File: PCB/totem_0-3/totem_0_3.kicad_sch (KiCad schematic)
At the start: 88 parts, among them J1 MJ-4PP-9, J2 MJ-4PP-9, U1 xiao-ble, U2 xiao-ble

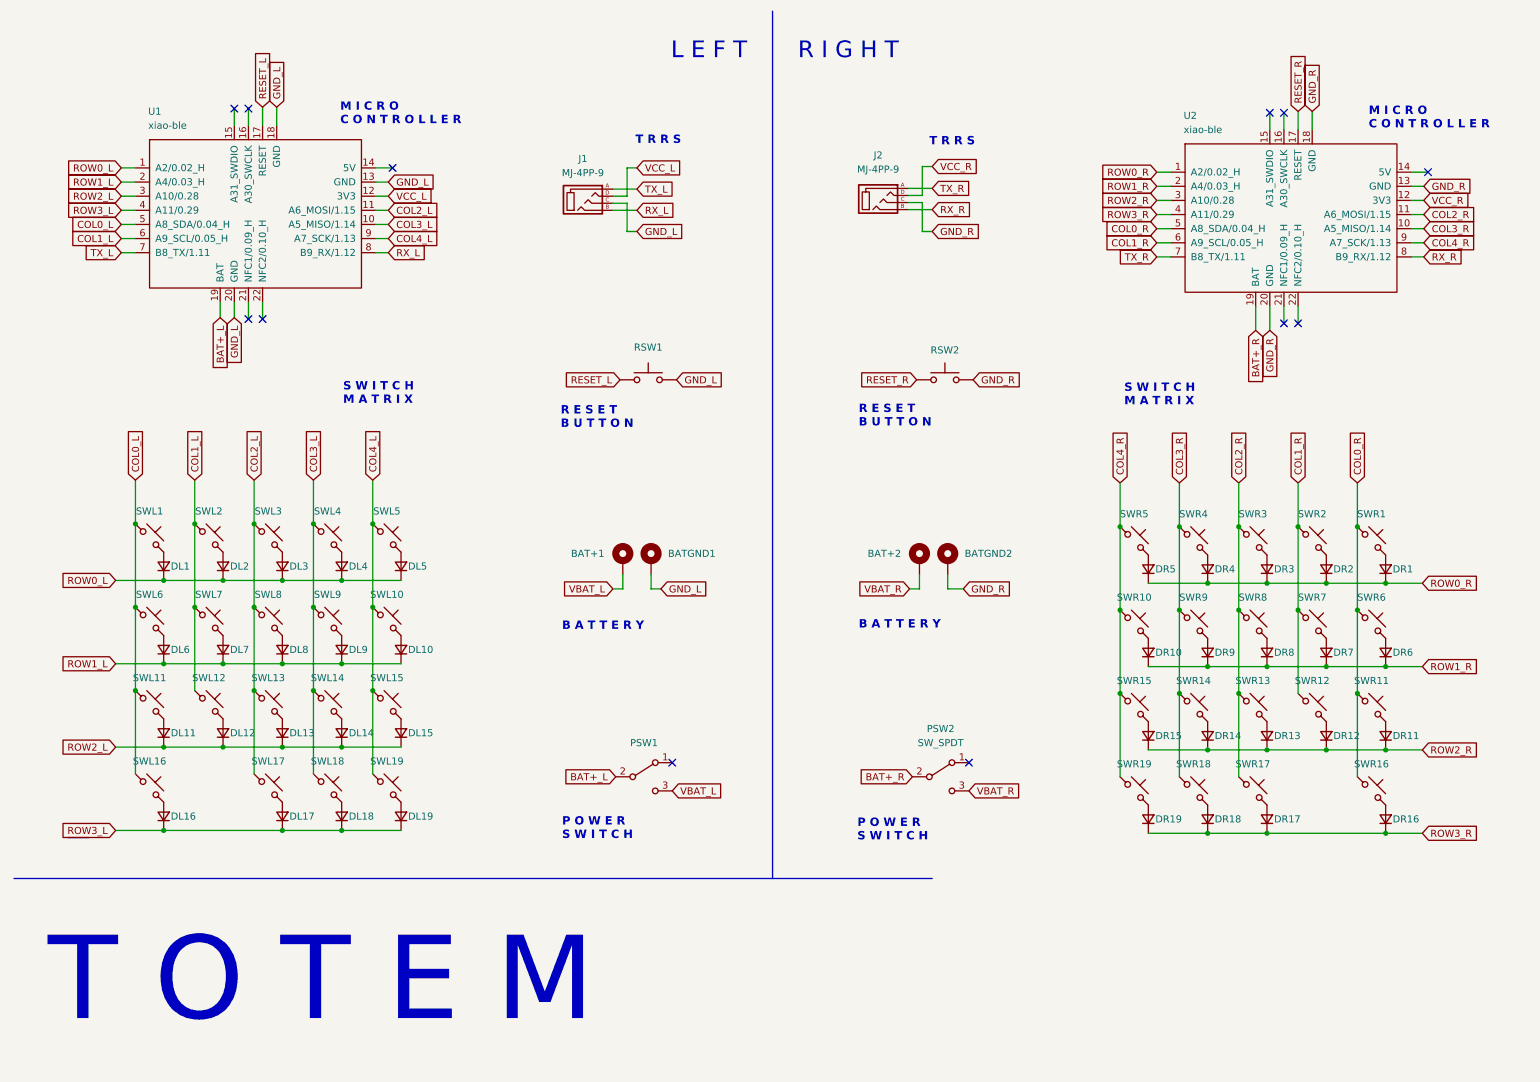
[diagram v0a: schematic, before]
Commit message: Modded for nice-nano
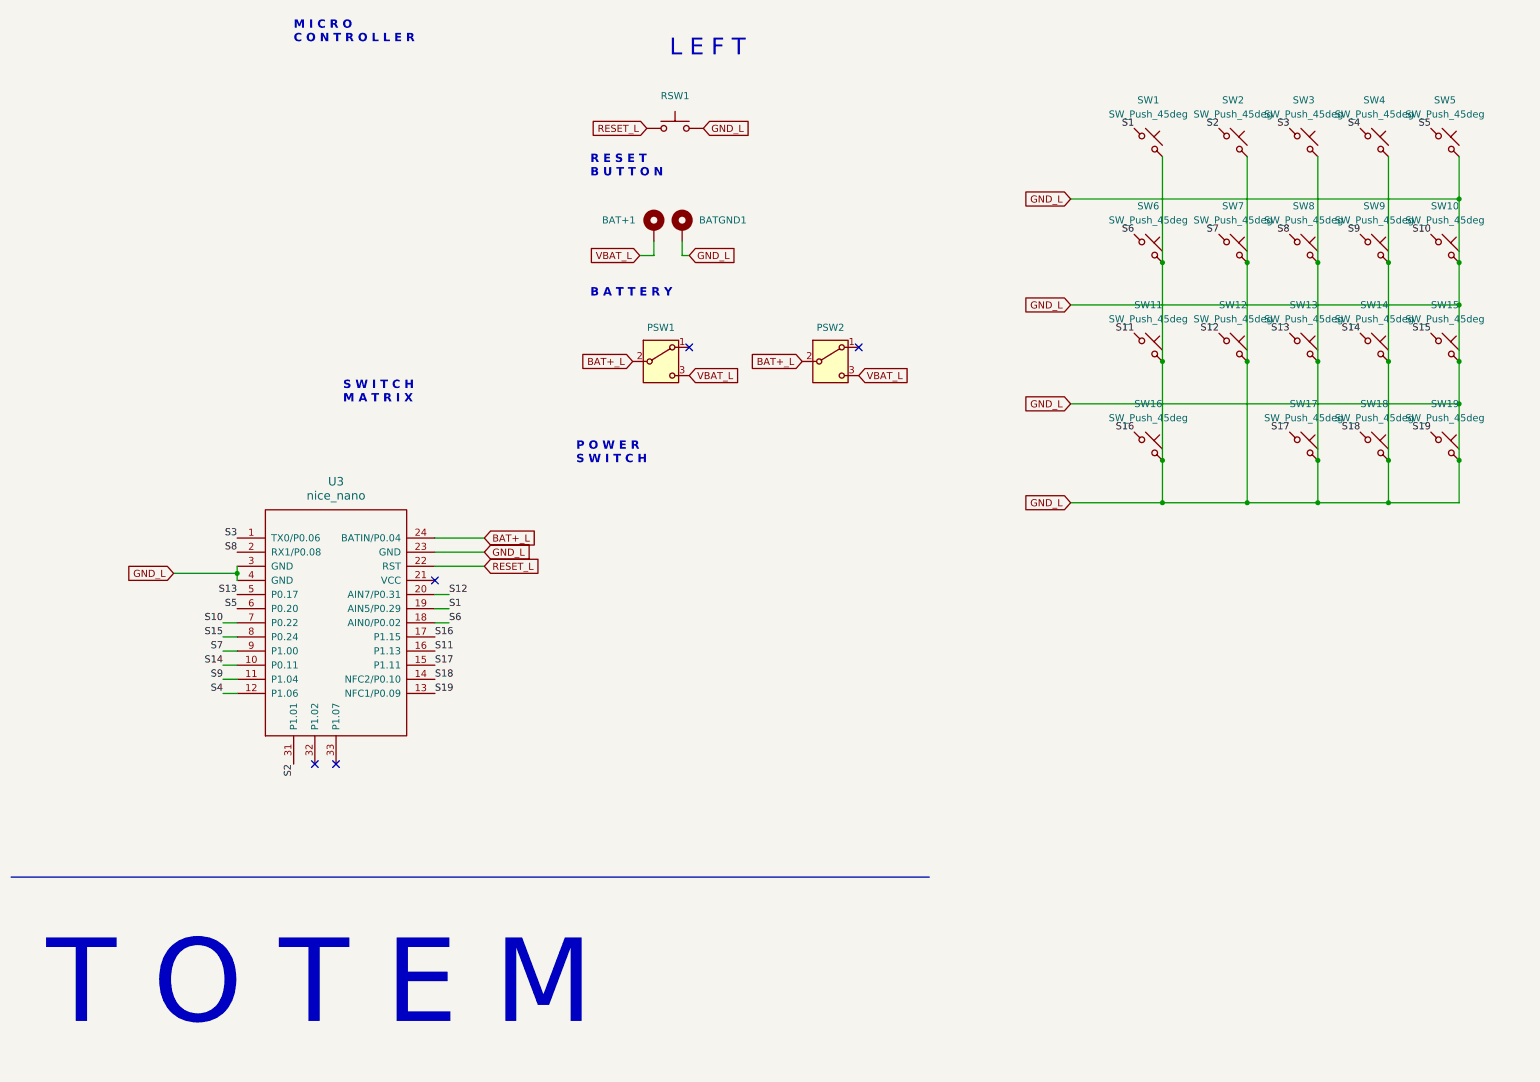
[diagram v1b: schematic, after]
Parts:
- removed BAT+2: +, TOTEMlib:BatteryPad, symbol Mechanical:MountingHole_Pad
- removed BATGND2: -, TOTEMlib:BatteryPad, symbol Mechanical:MountingHole_Pad
- removed DL1, DL10, DL11, DL12, DL13, DL14, DL15, DL16, DL17, DL18, DL19, DL2, DL3, DL4, DL5, DL6, DL7, DL8, DL9, DR1, DR10, DR11, DR12, DR13, DR14, DR15, DR16, DR17, DR18, DR19, DR2, DR3, DR4, DR5, DR6, DR7, DR8, DR9: D_Small, TOTEMlib:Diode_SOD123, symbol Device:D_Small
- removed J1, J2: MJ-4PP-9, TOTEMlib:MJ-4PP-9_1side, symbol kbd:MJ-4PP-9
- removed RSW2: SW_Push, TOTEMlib:SKHLLCA010, symbol Switch:SW_Push
- removed SWL1, SWL10, SWL11, SWL12, SWL13, SWL14, SWL15, SWL16, SWL17, SWL18, SWL19, SWL2, SWL3, SWL4, SWL5, SWL6, SWL7, SWL8, SWL9, SWR1, SWR10, SWR11, SWR12, SWR13, SWR14, SWR15, SWR16, SWR17, SWR18, SWR19, SWR2, SWR3, SWR4, SWR5, SWR6, SWR7, SWR8, SWR9: SW_Push_45deg, TOTEMlib:Kailh_socket_PG1350_optional, symbol Switch:SW_Push_45deg
- removed U1, U2: xiao-ble, TOTEMlib:xiao-ble-smd-cutout, symbol mcu:xiao-ble
- added SW1, SW10, SW11, SW12, SW13, SW14, SW15, SW16, SW17, SW18, SW19, SW2, SW3, SW4, SW5, SW6, SW7, SW8, SW9: SW_Push_45deg, switches:Kailh_socket_PG1350_reversible, symbol Switch:SW_Push_45deg
- added U3: nice_nano, nice-nano:nice_nano, symbol nice-nano:nice_nano
- BAT+1, BATGND1: now left out of the parts list
- RSW1: footprint TOTEMlib:SKHLLCA010 -> kbd:ResetSW
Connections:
- net BAT+_R is gone; now on net BAT+_L: PSW2.2 (B)
- net VBAT_R is gone; now on net VBAT_L: PSW2.3 (C)
- net BAT+_L: now also U3.24 (BATIN/P0.04)
- net GND_L: now also SW1.2, SW10.2, SW11.2, SW12.2, SW13.2, SW14.2, SW15.2, SW16.2, SW17.2, SW18.2, SW19.2, SW2.2, SW3.2, SW4.2, SW5.2, SW6.2, SW7.2, SW8.2, SW9.2, U3.23 (GND), U3.3 (GND), U3.4 (GND)
- net RESET_L: now also U3.22 (RST)
- new net S1: SW1.1, U3.19 (AIN5/P0.29)
- new net S10: SW10.1, U3.7 (P0.22)
- new net S11: SW11.1, U3.16 (P1.13)
- new net S12: SW12.1, U3.20 (AIN7/P0.31)
- new net S13: SW13.1, U3.5 (P0.17)
- new net S14: SW14.1, U3.10 (P0.11)
- new net S15: SW15.1, U3.8 (P0.24)
- new net S16: SW16.1, U3.17 (P1.15)
- new net S17: SW17.1, U3.15 (P1.11)
- new net S18: SW18.1, U3.14 (NFC2/P0.10)
- new net S19: SW19.1, U3.13 (NFC1/P0.09)
- new net S2: SW2.1, U3.31 (P1.01)
- new net S3: SW3.1, U3.1 (TX0/P0.06)
- new net S4: SW4.1, U3.12 (P1.06)
- new net S5: SW5.1, U3.6 (P0.20)
- new net S6: SW6.1, U3.18 (AIN0/P0.02)
- new net S7: SW7.1, U3.9 (P1.00)
- new net S8: SW8.1, U3.2 (RX1/P0.08)
- new net S9: SW9.1, U3.11 (P1.04)
- no-connect marks 12 -> 5
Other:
- note removed: "R I G H T"
- note removed: "T R R S"
- moved on the sheet: BAT+1, BATGND1, RSW1
